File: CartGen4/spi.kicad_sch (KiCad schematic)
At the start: 6 parts

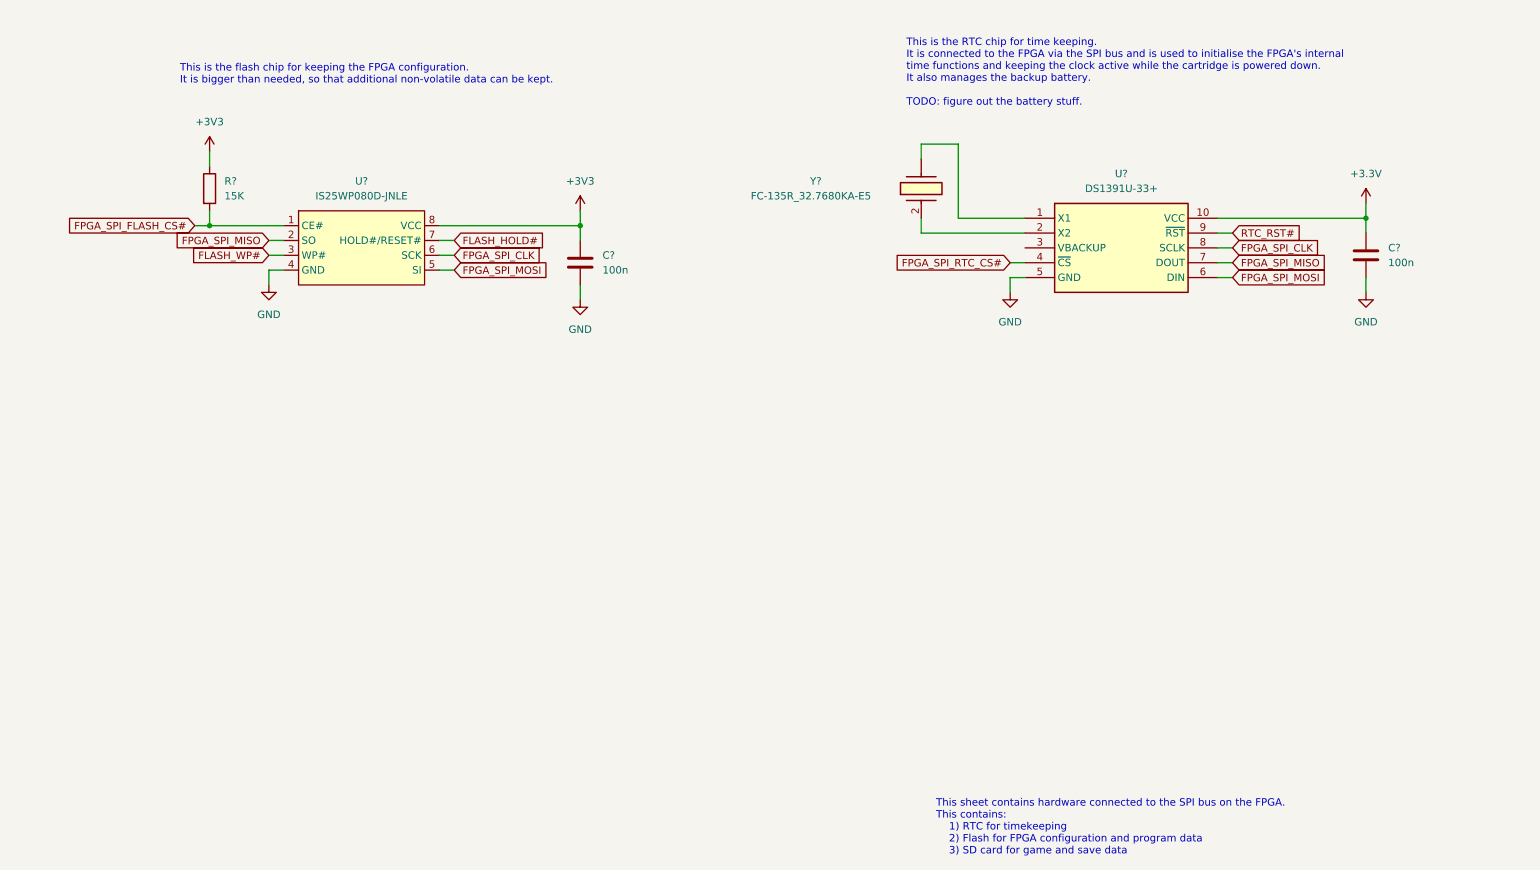
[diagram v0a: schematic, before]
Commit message: Added SD card holder
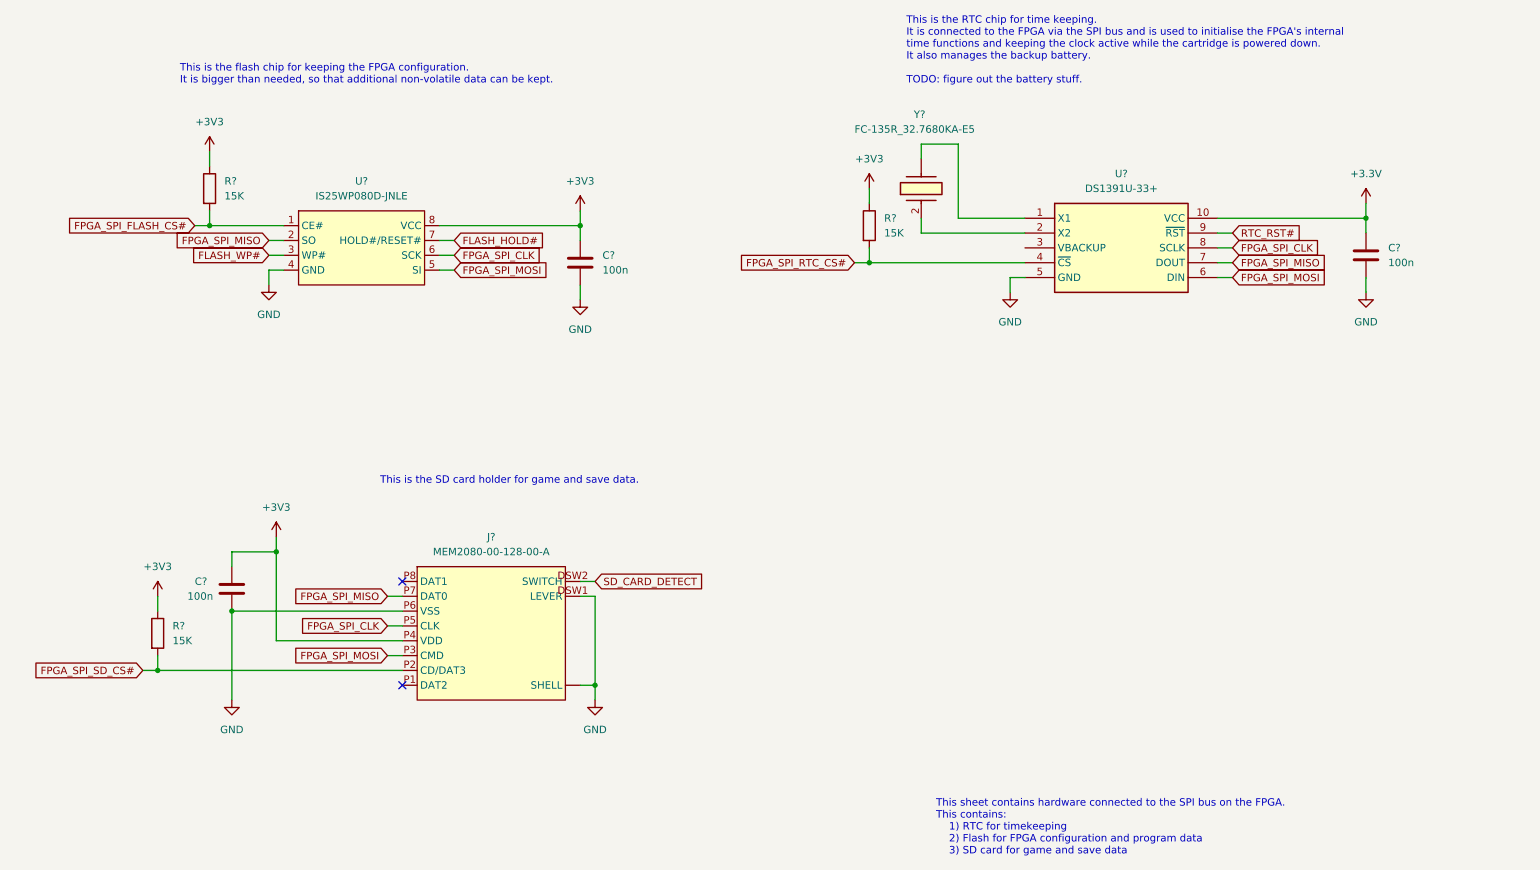
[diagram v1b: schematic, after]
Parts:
- added C?: 100n, symbol Device:C
- added J?: MEM2080-00-128-00-A, symbol SamacSys_Parts:MEM2080-00-128-00-A
- added R? (x2): 15K, symbol Device:R
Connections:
- net +3V3: now also C?.1, J?.P4 (VDD), R?.1, R?.1
- net FPGA_SPI_CLK: now also J?.P5 (CLK)
- net FPGA_SPI_MISO: now also J?.P7 (DAT0)
- net FPGA_SPI_MOSI: now also J?.P3 (CMD)
- net FPGA_SPI_RTC_CS#: now also R?.2
- net GND: now also C?.2, J?. (SHELL), J?.DSW1 (LEVER), J?.P6 (VSS)
- new net FPGA_SPI_SD_CS#: J?.P2 (CD/DAT3), R?.2
- new net SD_CARD_DETECT: J?.DSW2 (SWITCH)
- no-connect marks 0 -> 2
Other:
- note added: "This is the SD card holder for game and save data."

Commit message: Added copyright
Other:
- company: (none) -> © Elijah Almeida Coimbra
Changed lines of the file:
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@@
   (title_block
     (title "SPI bus and peripherals")
+    (company "© Elijah Almeida Coimbra")
   )
   (junction (at 120.65 148.59) (diameter 0) (color 0 0 0 0)

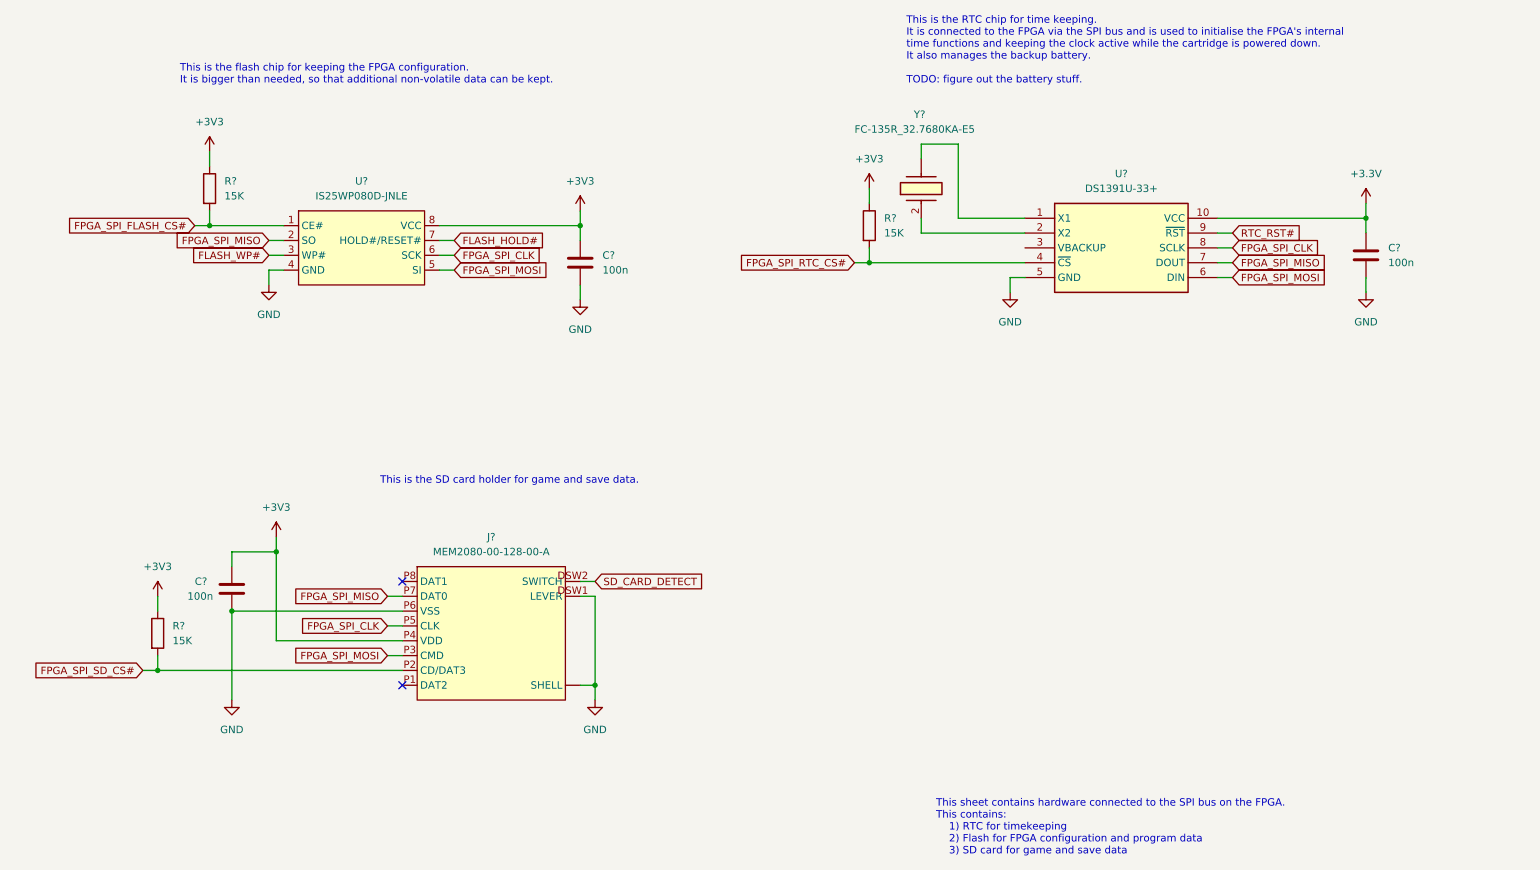
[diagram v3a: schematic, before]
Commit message: Added reference designators to everything
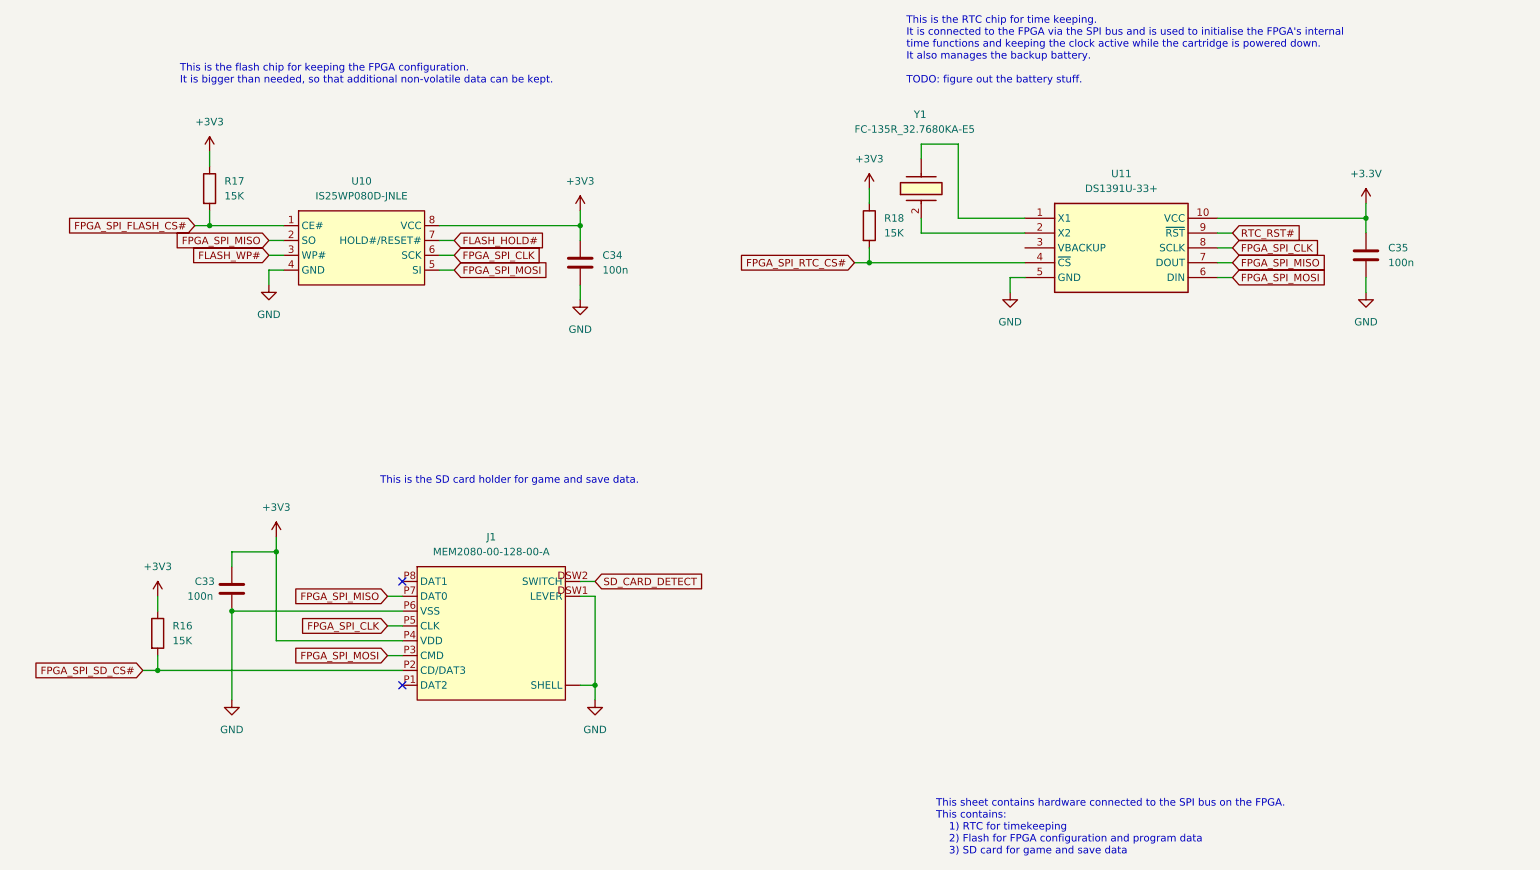
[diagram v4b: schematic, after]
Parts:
- gave numbers to parts that had none: 10
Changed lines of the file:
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@@
   (symbol (lib_id "power:+3V3") (at 66.04 123.19 0) (unit 1)
     (in_bom yes) (on_board yes) (fields_autoplaced)
-    (property "Reference" "#PWR?" (id 0) (at 66.04 127 0)
+    (property "Reference" "#PWR077" (id 0) (at 66.04 127 0)
       (effects (font (size 1.27 1.27)) hide)
     )
@@
   (symbol (lib_id "power:GND") (at 191.77 81.28 0) (unit 1)
     (in_bom yes) (on_board yes) (fields_autoplaced)
-    (property "Reference" "#PWR?" (id 0) (at 191.77 87.63 0)
+    (property "Reference" "#PWR082" (id 0) (at 191.77 87.63 0)
       (effects (font (size 1.27 1.27)) hide)
     )
@@
   (symbol (lib_id "Device:R") (at 167.64 69.85 0) (unit 1)
     (in_bom yes) (on_board yes) (fields_autoplaced)
-    (property "Reference" "R?" (id 0) (at 170.18 68.5799 0)
+    (property "Reference" "R18" (id 0) (at 170.18 68.5799 0)
       (effects (font (size 1.27 1.27)) (justify left))
     )
@@
   (symbol (lib_id "SamacSys_Parts:MEM2080-00-128-00-A") (at 87.63 132.08 0) (unit 1)
     (in_bom yes) (on_board yes) (fields_autoplaced)
-    (property "Reference" "J?" (id 0) (at 102.87 123.19 0))
+    (property "Reference" "J1" (id 0) (at 102.87 123.19 0))
     (property "Value" "MEM2080-00-128-00-A" (id 1) (at 102.87 125.73 0))
     (property "Footprint" "" (id 2) (at 87.63 148.59 0)
@@
   (symbol (lib_id "power:GND") (at 120.65 151.13 0) (unit 1)
     (in_bom yes) (on_board yes) (fields_autoplaced)
-    (property "Reference" "#PWR?" (id 0) (at 120.65 157.48 0)
+    (property "Reference" "#PWR080" (id 0) (at 120.65 157.48 0)
       (effects (font (size 1.27 1.27)) hide)
     )
@@
   (symbol (lib_id "Device:C") (at 118.11 76.2 0) (unit 1)
     (in_bom yes) (on_board yes) (fields_autoplaced)
-    (property "Reference" "C?" (id 0) (at 121.92 74.9299 0)
+    (property "Reference" "C34" (id 0) (at 121.92 74.9299 0)
       (effects (font (size 1.27 1.27)) (justify left))
     )
@@
   (symbol (lib_id "power:GND") (at 118.11 82.55 0) (unit 1)
     (in_bom yes) (on_board yes) (fields_autoplaced)
-    (property "Reference" "#PWR?" (id 0) (at 118.11 88.9 0)
+    (property "Reference" "#PWR079" (id 0) (at 118.11 88.9 0)
       (effects (font (size 1.27 1.27)) hide)
     )
@@
   (symbol (lib_id "power:GND") (at 58.42 151.13 0) (unit 1)
     (in_bom yes) (on_board yes) (fields_autoplaced)
-    (property "Reference" "#PWR?" (id 0) (at 58.42 157.48 0)
+    (property "Reference" "#PWR075" (id 0) (at 58.42 157.48 0)
       (effects (font (size 1.27 1.27)) hide)
     )
@@
   (symbol (lib_id "Device:C") (at 58.42 132.08 0) (unit 1)
     (in_bom yes) (on_board yes)
-    (property "Reference" "C?" (id 0) (at 52.07 130.81 0)
+    (property "Reference" "C33" (id 0) (at 52.07 130.81 0)
       (effects (font (size 1.27 1.27)) (justify left))
     )
@@
   (symbol (lib_id "SamacSys_Parts:FC-135R_32.7680KA-E5") (at 176.53 68.58 90) (unit 1)
     (in_bom yes) (on_board yes)
-    (property "Reference" "Y?" (id 0) (at 175.26 50.8 90)
+    (property "Reference" "Y1" (id 0) (at 175.26 50.8 90)
       (effects (font (size 1.27 1.27)) (justify right))
     )
@@
   (symbol (lib_id "Device:R") (at 45.72 139.7 0) (unit 1)
     (in_bom yes) (on_board yes) (fields_autoplaced)
-    (property "Reference" "R?" (id 0) (at 48.26 138.4299 0)
+    (property "Reference" "R16" (id 0) (at 48.26 138.4299 0)
       (effects (font (size 1.27 1.27)) (justify left))
     )
@@
   (symbol (lib_id "power:+3V3") (at 45.72 133.35 0) (unit 1)
     (in_bom yes) (on_board yes) (fields_autoplaced)
-    (property "Reference" "#PWR?" (id 0) (at 45.72 137.16 0)
+    (property "Reference" "#PWR073" (id 0) (at 45.72 137.16 0)
       (effects (font (size 1.27 1.27)) hide)
     )
@@
   (symbol (lib_id "power:+3V3") (at 118.11 67.31 0) (unit 1)
     (in_bom yes) (on_board yes) (fields_autoplaced)
-    (property "Reference" "#PWR?" (id 0) (at 118.11 71.12 0)
+    (property "Reference" "#PWR078" (id 0) (at 118.11 71.12 0)
       (effects (font (size 1.27 1.27)) hide)
     )
@@
   (symbol (lib_id "Device:C") (at 252.73 74.93 0) (unit 1)
     (in_bom yes) (on_board yes) (fields_autoplaced)
-    (property "Reference" "C?" (id 0) (at 256.54 73.6599 0)
+    (property "Reference" "C35" (id 0) (at 256.54 73.6599 0)
       (effects (font (size 1.27 1.27)) (justify left))
     )
@@
   (symbol (lib_id "power:+3V3") (at 54.61 57.15 0) (unit 1)
     (in_bom yes) (on_board yes) (fields_autoplaced)
-    (property "Reference" "#PWR?" (id 0) (at 54.61 60.96 0)
+    (property "Reference" "#PWR074" (id 0) (at 54.61 60.96 0)
       (effects (font (size 1.27 1.27)) hide)
     )
@@
   (symbol (lib_id "SamacSys_Parts:IS25WP080D-JNLE") (at 67.31 69.85 0) (unit 1)
     (in_bom yes) (on_board yes) (fields_autoplaced)
-    (property "Reference" "U?" (id 0) (at 80.645 62.23 0))
+    (property "Reference" "U10" (id 0) (at 80.645 62.23 0))
     (property "Value" "IS25WP080D-JNLE" (id 1) (at 80.645 64.77 0))
     (property "Footprint" "" (id 2) (at 67.31 69.85 0)
@@
   (symbol (lib_id "power:+3.3V") (at 252.73 66.04 0) (unit 1)
     (in_bom yes) (on_board yes) (fields_autoplaced)
-    (property "Reference" "#PWR?" (id 0) (at 252.73 69.85 0)
+    (property "Reference" "#PWR083" (id 0) (at 252.73 69.85 0)
       (effects (font (size 1.27 1.27)) hide)
     )
@@
   (symbol (lib_id "power:+3V3") (at 167.64 63.5 0) (unit 1)
     (in_bom yes) (on_board yes) (fields_autoplaced)
-    (property "Reference" "#PWR?" (id 0) (at 167.64 67.31 0)
+    (property "Reference" "#PWR081" (id 0) (at 167.64 67.31 0)
       (effects (font (size 1.27 1.27)) hide)
     )
@@
   (symbol (lib_id "power:GND") (at 64.77 80.01 0) (unit 1)
     (in_bom yes) (on_board yes) (fields_autoplaced)
-    (property "Reference" "#PWR?" (id 0) (at 64.77 86.36 0)
+    (property "Reference" "#PWR076" (id 0) (at 64.77 86.36 0)
       (effects (font (size 1.27 1.27)) hide)
     )
@@
   (symbol (lib_id "SamacSys_Parts:DS1391U-33+") (at 194.31 68.58 0) (unit 1)
     (in_bom yes) (on_board yes) (fields_autoplaced)
-    (property "Reference" "U?" (id 0) (at 210.82 60.96 0))
+    (property "Reference" "U11" (id 0) (at 210.82 60.96 0))
     (property "Value" "DS1391U-33+" (id 1) (at 210.82 63.5 0))
     (property "Footprint" "" (id 2) (at 194.31 68.58 0)
@@
   (symbol (lib_id "power:GND") (at 252.73 81.28 0) (unit 1)
     (in_bom yes) (on_board yes) (fields_autoplaced)
-    (property "Reference" "#PWR?" (id 0) (at 252.73 87.63 0)
+    (property "Reference" "#PWR084" (id 0) (at 252.73 87.63 0)
       (effects (font (size 1.27 1.27)) hide)
     )
@@
   (symbol (lib_id "Device:R") (at 54.61 63.5 0) (unit 1)
     (in_bom yes) (on_board yes) (fields_autoplaced)
-    (property "Reference" "R?" (id 0) (at 57.15 62.2299 0)
-      (effects (font (size 1.27 1.27)) (justify left))
-    )
+    (property "Reference" "R17" (id 0) (at 57.15 62.2299 0)
+      (effects (font (size 1.27 1.27)) (justify left))
+    )

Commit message: Fixed DRC
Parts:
- added BT1: Battery_Cell, symbol Device:Battery_Cell
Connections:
- net GND: now also BT1.2 (-)
- net at U11.3 (VBACKUP): now also BT1.1 (+)
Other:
- note added: "This is the RTC chip for time keeping. It is connected to the FPGA via the SPI bus and is used to initialise the FPGA's internal time functions and keeping the clock active while the cartridge is powered down. It also manages the backup battery."
- note removed: "This is the RTC chip for time keeping. It is connected to the FPGA via the SPI bus and is used to initialise the FPGA's internal time functions and keeping the clock active while the cartridge is powered down. It also manages the backup battery. TODO: figure out the battery stuff."
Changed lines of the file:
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@@
+    (stroke (width 0) (type default) (color 0 0 0 0))
+  )
+  (wire (pts (xy 184.15 90.17) (xy 184.15 73.66))
     (stroke (width 0) (type default) (color 0 0 0 0))
   )
@@
     (stroke (width 0) (type default) (color 0 0 0 0))
   )
+  (wire (pts (xy 184.15 73.66) (xy 194.31 73.66))
+    (stroke (width 0) (type default) (color 0 0 0 0))
+  )
   (wire (pts (xy 45.72 133.35) (xy 45.72 135.89))
     (stroke (width 0) (type default) (color 0 0 0 0))
@@
     (stroke (width 0) (type default) (color 0 0 0 0))
   )
+  (wire (pts (xy 184.15 97.79) (xy 184.15 100.33))
+    (stroke (width 0) (type default) (color 0 0 0 0))
+  )
   (wire (pts (xy 120.65 133.35) (xy 120.65 148.59))
     (stroke (width 0) (type default) (color 0 0 0 0))
@@
     (stroke (width 0) (type default) (color 0 0 0 0))
   )
-  (text "This is the RTC chip for time keeping.\nIt is connected to the FPGA via the SPI bus and is used to initialise the FPGA's internal\ntime functions and keeping the clock active while the cartridge is powered down.\nIt also manages the backup battery.\n\nTODO: figure out the battery stuff."
+  (text "This is the RTC chip for time keeping.\nIt is connected to the FPGA via the SPI bus and is used to initialise the FPGA's internal\ntime functions and keeping the clock active while the cartridge is powered down.\nIt also manages the backup battery."
     (at 173.99 45.72 0)
     (effects (font (size 1.27 1.27)) (justify left bottom))
@@
     (pin "1")
   )
+  (symbol (lib_id "power:GND") (at 184.15 100.33 0) (unit 1)
+    (in_bom yes) (on_board yes) (fields_autoplaced)
+    (property "Reference" "#PWR0101" (id 0) (at 184.15 106.68 0)
+      (effects (font (size 1.27 1.27)) hide)
+    )
+    (property "Value" "GND" (id 1) (at 184.15 105.41 0))
+    (property "Footprint" "" (id 2) (at 184.15 100.33 0)
+      (effects (font (size 1.27 1.27)) hide)
+    )
+    (property "Datasheet" "" (id 3) (at 184.15 100.33 0)
+      (effects (font (size 1.27 1.27)) hide)
+    )
+    (pin "1")
+  )
   (symbol (lib_id "SamacSys_Parts:IS25WP080D-JNLE") (at 67.31 69.85 0) (unit 1)
     (in_bom yes) (on_board yes) (fields_autoplaced)
@@
     (pin "9")
   )
+  (symbol (lib_id "Device:Battery_Cell") (at 184.15 95.25 0) (unit 1)
+    (in_bom yes) (on_board yes) (fields_autoplaced)
+    (property "Reference" "BT1" (id 0) (at 187.96 91.9479 0)
+      (effects (font (size 1.27 1.27)) (justify left))
+    )
+    (property "Value" "Battery_Cell" (id 1) (at 187.96 94.4879 0)
+      (effects (font (size 1.27 1.27)) (justify left))
+    )
+    (property "Footprint" "" (id 2) (at 184.15 93.726 90)
+      (effects (font (size 1.27 1.27)) hide)
+    )
+    (property "Datasheet" "~" (id 3) (at 184.15 93.726 90)
+      (effects (font (size 1.27 1.27)) hide)
+    )
+    (pin "1")
+    (pin "2")
+  )
   (symbol (lib_id "power:GND") (at 252.73 81.28 0) (unit 1)
